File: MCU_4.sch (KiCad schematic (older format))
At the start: 18 parts, among them U2 STM32F051K6Ux

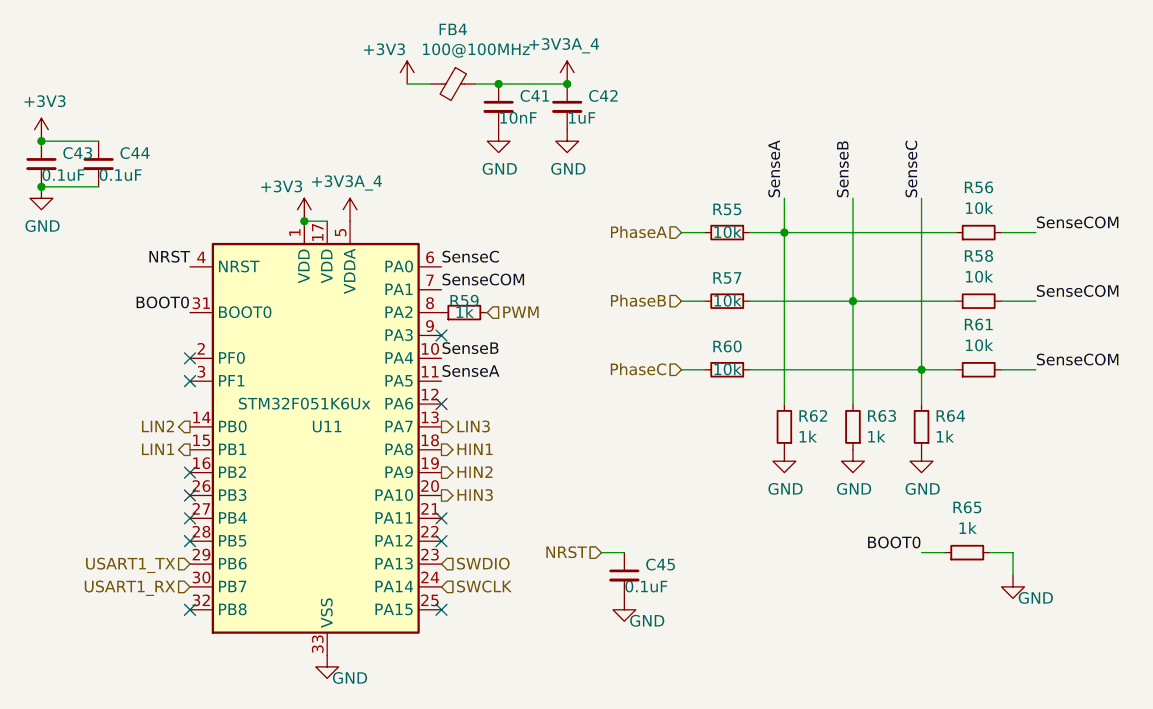
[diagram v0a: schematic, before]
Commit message: Lots of changes made with back being rerouted
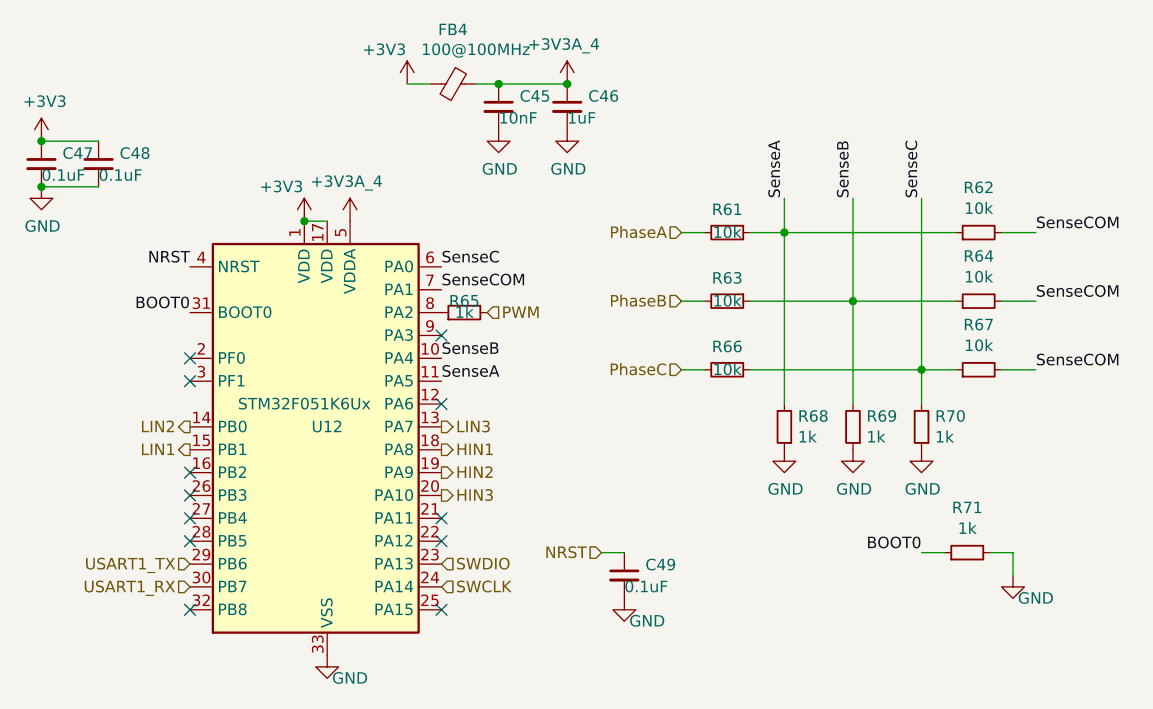
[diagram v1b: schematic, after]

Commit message: Added stuff
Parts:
- removed R24: 1k, Resistor_SMD:R_0402_1005Metric, symbol Device:R_Small
- removed U2: STM32F051K6Ux, Package_DFN_QFN:QFN-32-1EP_5x5mm_P0.5mm_EP3.45x3.45mm, symbol MCU_ST_STM32F0:STM32F051K6Ux
- added R65: 1k, Resistor_SMD:R_0402_1005Metric, symbol Device:R_Small
- added U12: STM32F051K6Ux, Package_DFN_QFN:QFN-32-1EP_5x5mm_P0.5mm_EP3.45x3.45mm, symbol MCU_ST_STM32F0:STM32F051K6Ux
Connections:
- net +3.3VA_4: now also U12.5 (VDDA)
- net +3V3: now also U12.1 (VDD), U12.17 (VDD)
- net BOOT0: now also U12.31 (BOOT0)
- net GND: now also U12.33 (VSS)
- net HIN1: now also U12.18 (PA8)
- net HIN2: now also U12.19 (PA9)
- net HIN3: now also U12.20 (PA10)
- net LIN1: now also U12.15 (PB1)
- net LIN2: now also U12.14 (PB0)
- net LIN3: now also U12.13 (PA7)
- net NRST: now also U12.4 (NRST)
- net PWM: now also R65.2
- net SWCLK: now also U12.24 (PA14)
- net SWDIO: now also U12.23 (PA13)
- net SenseA: now also U12.11 (PA5)
- net SenseB: now also U12.10 (PA4)
- net SenseC: now also U12.6 (PA0)
- net SenseCOM: now also U12.7 (PA1)
- net USART1_RX: now also U12.30 (PB7)
- net USART1_TX: now also U12.29 (PB6)
- new net: R65.1, U12.8 (PA2)
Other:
- moved on the sheet: C49
